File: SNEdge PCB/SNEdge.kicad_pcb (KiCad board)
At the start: 2 copper layers, 38.2 x 19.3 mm, 41 parts, among them J1 RGB_OUT, U1 THS7376

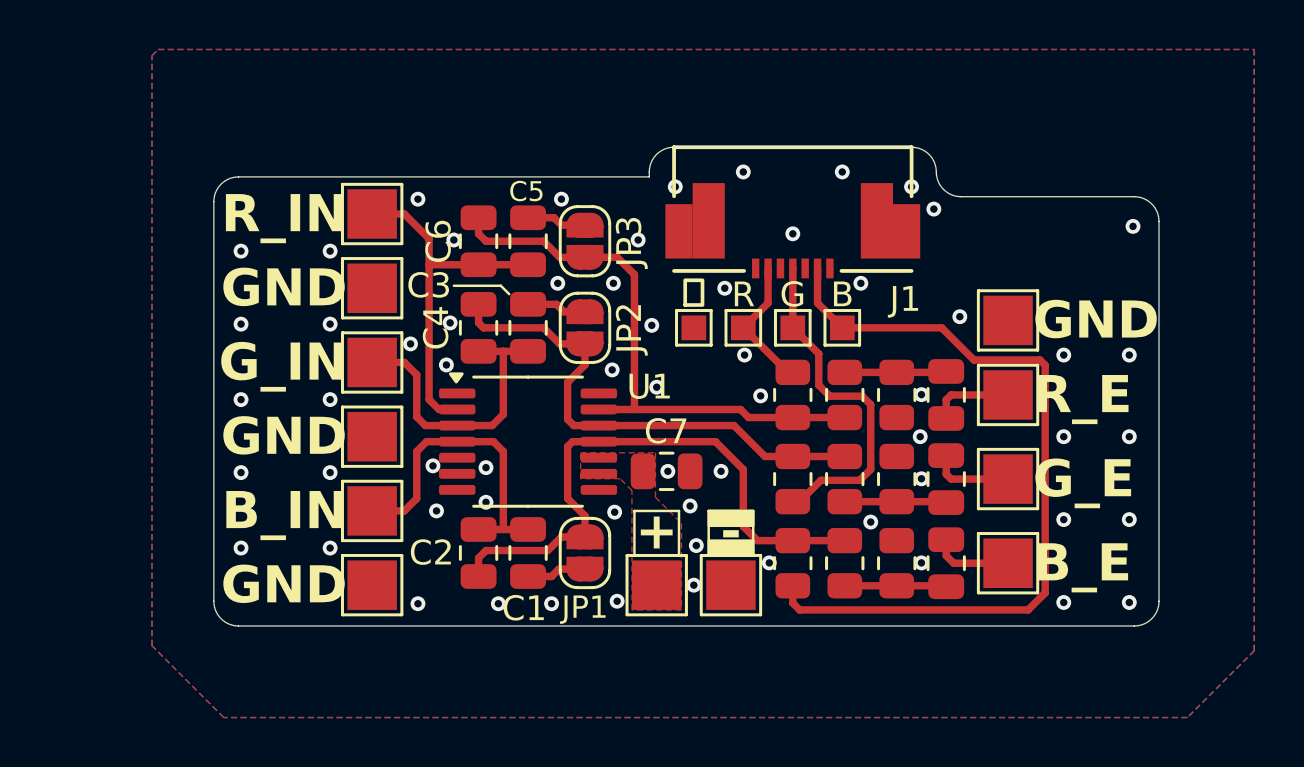
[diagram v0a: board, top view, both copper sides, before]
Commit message: AC coupled input, SD filter enabled
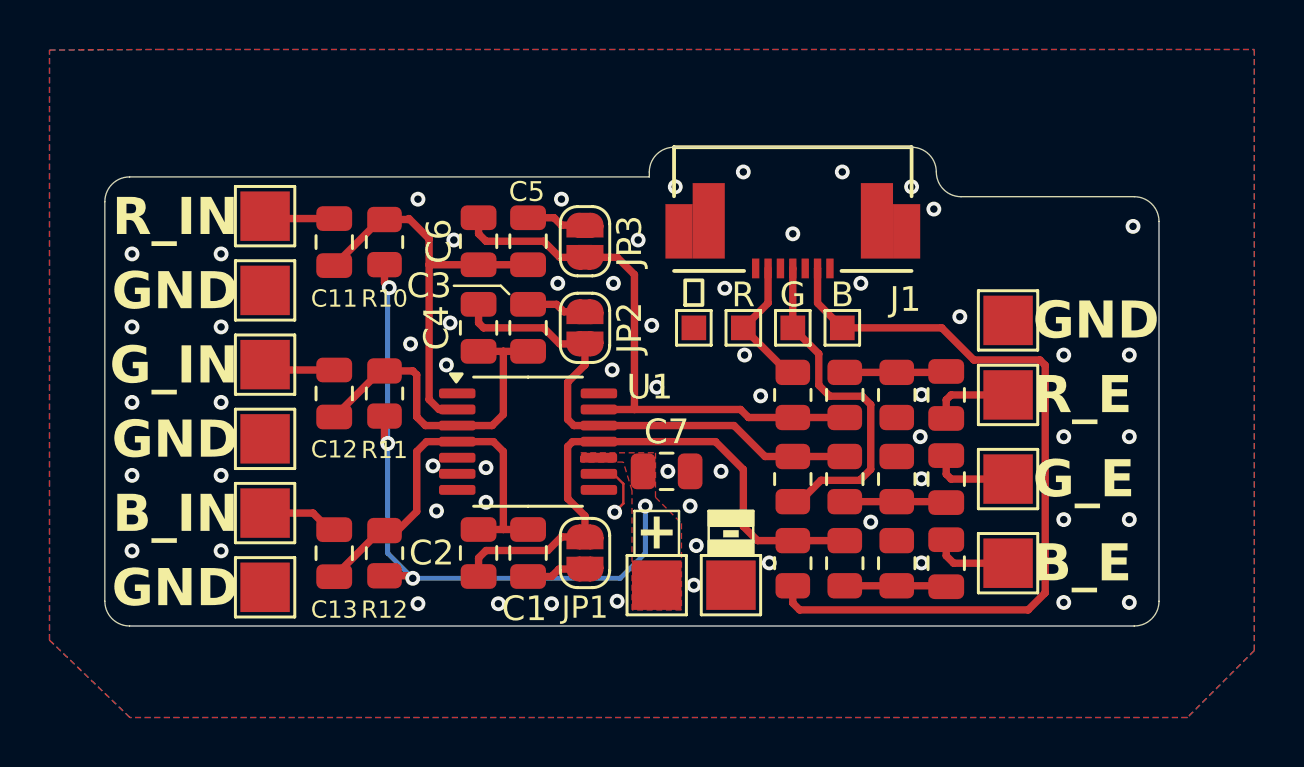
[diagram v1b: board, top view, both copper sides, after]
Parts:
- removed REF**: OSHW-Logo_7.5x8mm_SilkScreen, Symbol:OSHW-Logo_7.5x8mm_SilkScreen
- added C11: 0.1uF, Capacitor_SMD:C_0805_2012Metric, F.Cu at (121.7, 94.2)
- added C12: 0.1uF, Capacitor_SMD:C_0805_2012Metric, F.Cu at (121.7, 100.4)
- added C13: 0.1uF, Capacitor_SMD:C_0805_2012Metric, F.Cu at (121.7, 106.8)
- added R10: 5M, Resistor_SMD:R_0805_2012Metric, F.Cu at (123.7, 94.2)
- added R11: 5M, Resistor_SMD:R_0805_2012Metric, F.Cu at (123.7, 100.4)
- added R12: 5M, Resistor_SMD:R_0805_2012Metric, F.Cu at (123.7, 106.8)
- C7: value 100nF -> 0.1uF
- moved TP3 4.33 mm to (118.9, 102.2)
- moved TP4 4.33 mm to (118.9, 96.2)
- moved TP5 4.33 mm to (118.9, 93.2)
- moved TP6 4.33 mm to (118.9, 99.2)
- moved TP7 4.33 mm to (118.9, 105.2)
- moved TP8 4.33 mm to (118.9, 108.2)
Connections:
- TP5 pad 1: Net-(U1-CH2_IN) -> Net-(C11-Pad1)
- TP6 pad 1: Net-(U1-CH3_IN) -> Net-(C12-Pad1)
- TP7 pad 1: Net-(U1-CH4_IN) -> Net-(C13-Pad1)
- U1 pad 9: VCC -> GND
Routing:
- net VCC: track 0.00 -> 27.3 mm, vias 0 -> 4
- net Net-(C13-Pad1): track 0.00 -> 3.12 mm
- net Net-(U1-CH4_IN): track 12.9 -> 15.8 mm
- net Net-(C12-Pad1): track 0.00 -> 2.94 mm
- net Net-(C11-Pad1): track 0.00 -> 2.83 mm
- net GND: track 0.10 -> 2.55 mm
- net Net-(U1-CH2_IN): track 14.5 -> 16.8 mm
- net Net-(U1-CH3_IN): track 12.1 -> 14.3 mm
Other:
- board size 38.2 x 19.3 mm -> 42.6 x 19.3 mm
